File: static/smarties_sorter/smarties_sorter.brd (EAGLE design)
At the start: 160 x 100 mm, 15 parts, among them IC1 MEGA8-P, Q1 16Mhz, Q2 IRLZ44Z

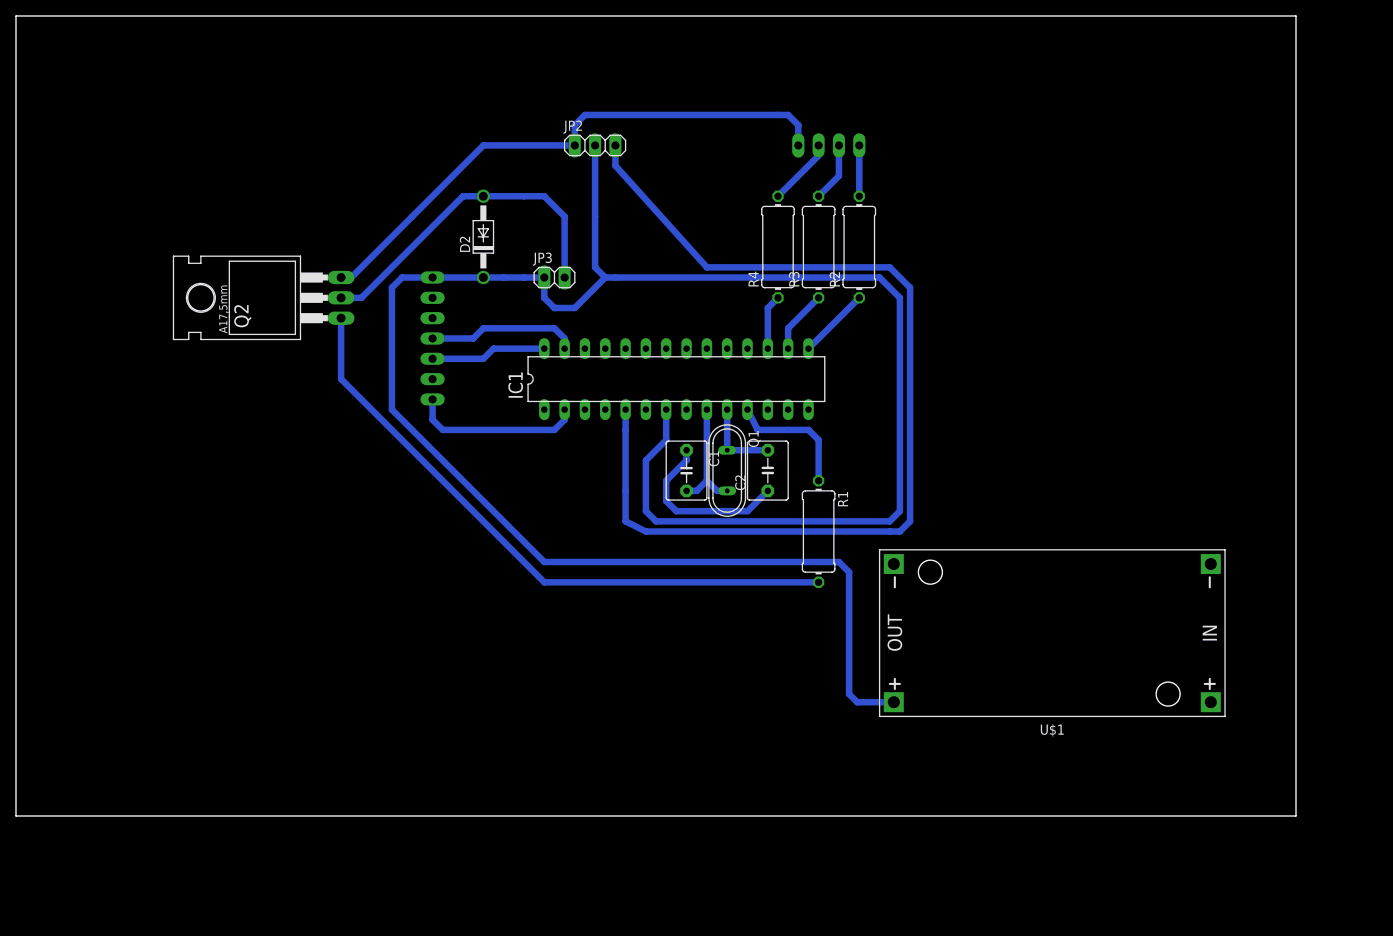
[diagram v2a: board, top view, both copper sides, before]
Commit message: [Smarties sorter] Adds screw clamp for battery
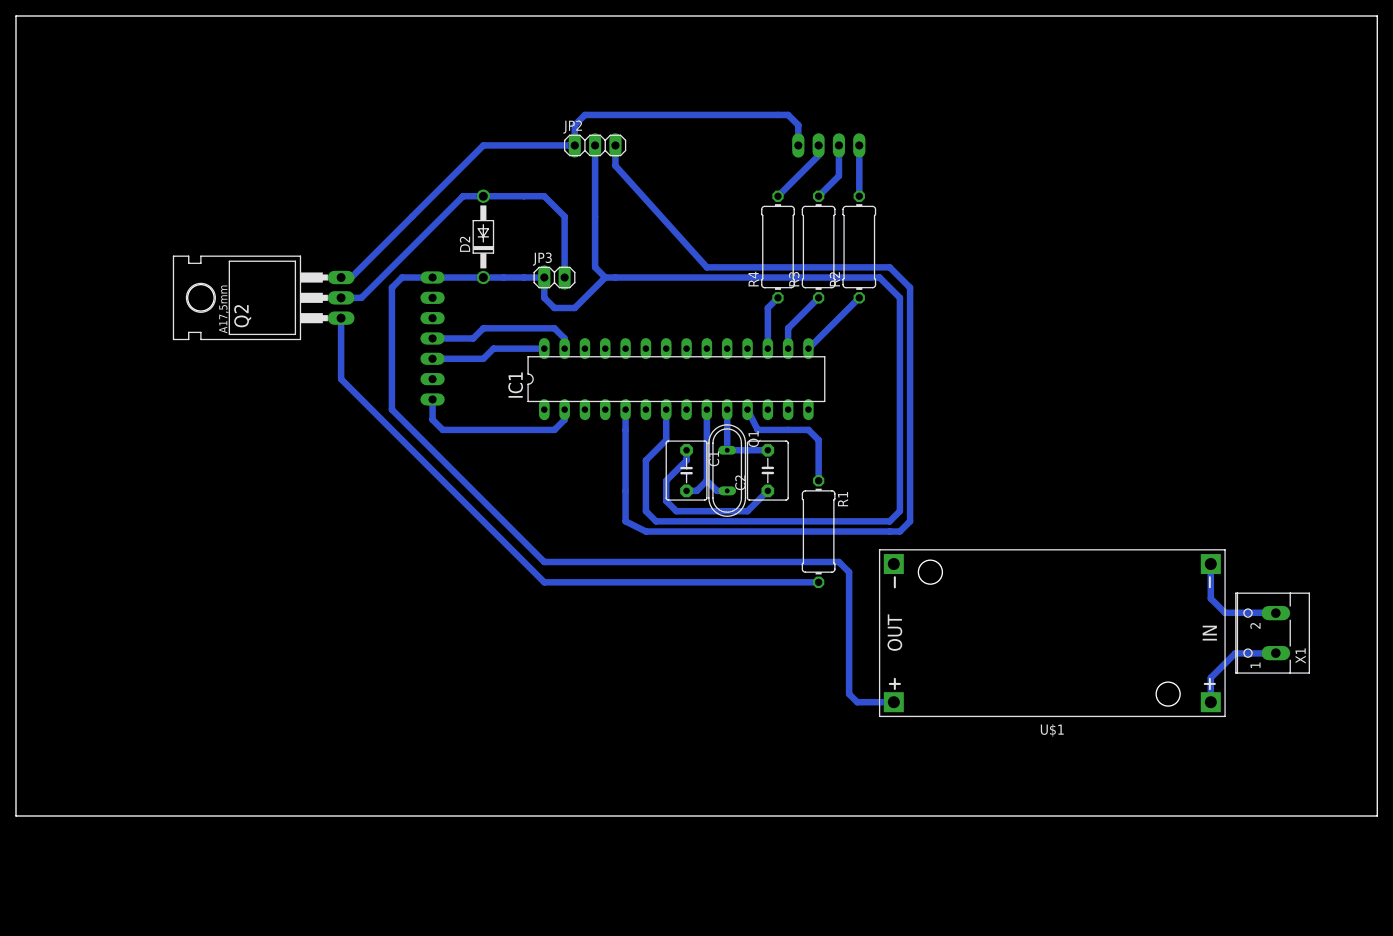
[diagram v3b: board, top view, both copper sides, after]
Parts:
- added X1: (no value), con-wago-500:W237-102
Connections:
- net 12V: now also X1.1
- net 12V_GND: now also X1.2
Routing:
- net 12V_GND: track 0.00 -> 13.2 mm
- net 12V: track 0.00 -> 12.5 mm
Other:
- board size 160 x 100 mm -> 170.2 x 100 mm
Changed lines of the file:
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@@
 <board>
 <plain>
-<wire x1="0" y1="0" x2="160" y2="0" width="0" layer="20"/>
-<wire x1="160" y1="0" x2="160" y2="100" width="0" layer="20"/>
-<wire x1="160" y1="100" x2="0" y2="100" width="0" layer="20"/>
+<wire x1="0" y1="0" x2="170.16" y2="0" width="0" layer="20"/>
+<wire x1="170.16" y1="0" x2="170.16" y2="100" width="0" layer="20"/>
+<wire x1="170.16" y1="100" x2="0" y2="100" width="0" layer="20"/>
 <wire x1="0" y1="100" x2="0" y2="0" width="0" layer="20"/>
 </plain>
@@
 <element name="D2" library="diode" package="DO41-10" value="1N4933" x="58.42" y="72.39" rot="R90"/>
 <element name="U$1" library="diy-modules" package="DC-DC-STEP-DOWN-LM2596" value="DC-DC-STEP-DOWN-LM2596" x="129.54" y="22.86" rot="R180"/>
+<element name="X1" library="con-wago-500" package="W237-102" value="" x="156.21" y="22.86" rot="R90">
+<attribute name="OC_NEWARK" value="70K9898" x="156.21" y="22.86" size="1.778" layer="27" rot="R90" display="off"/>
+<attribute name="MPN" value="237-102" x="156.21" y="22.86" size="1.778" layer="27" rot="R90" display="off"/>
+<attribute name="MF" value="" x="156.21" y="22.86" size="1.778" layer="27" rot="R90" display="off"/>
+<attribute name="OC_FARNELL" value="unknown" x="156.21" y="22.86" size="1.778" layer="27" rot="R90" display="off"/>
+</element>
 </elements>
 <signals>
@@
 <signal name="12V">
 <contactref element="U$1" pad="IN+"/>
+<contactref element="X1" pad="1"/>
+<wire x1="149.352" y1="14.224" x2="149.352" y2="17.272" width="0.8128" layer="16"/>
+<wire x1="149.352" y1="17.272" x2="152.4" y2="20.32" width="0.8128" layer="16"/>
+<wire x1="152.4" y1="20.32" x2="157.44" y2="20.32" width="0.8128" layer="16"/>
+<wire x1="157.44" y1="20.32" x2="157.48" y2="20.36" width="0.8128" layer="16"/>
 </signal>
 <signal name="12V_GND">
 <contactref element="U$1" pad="IN-"/>
+<contactref element="X1" pad="2"/>
+<wire x1="149.352" y1="31.496" x2="149.352" y2="27.178" width="0.8128" layer="16"/>
+<wire x1="149.352" y1="27.178" x2="151.13" y2="25.4" width="0.8128" layer="16"/>
+<wire x1="151.13" y1="25.4" x2="157.44" y2="25.4" width="0.8128" layer="16"/>
+<wire x1="157.44" y1="25.4" x2="157.48" y2="25.36" width="0.8128" layer="16"/>
 </signal>
 </signals>

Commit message: [Smarties Sorter] Adds ground plane.
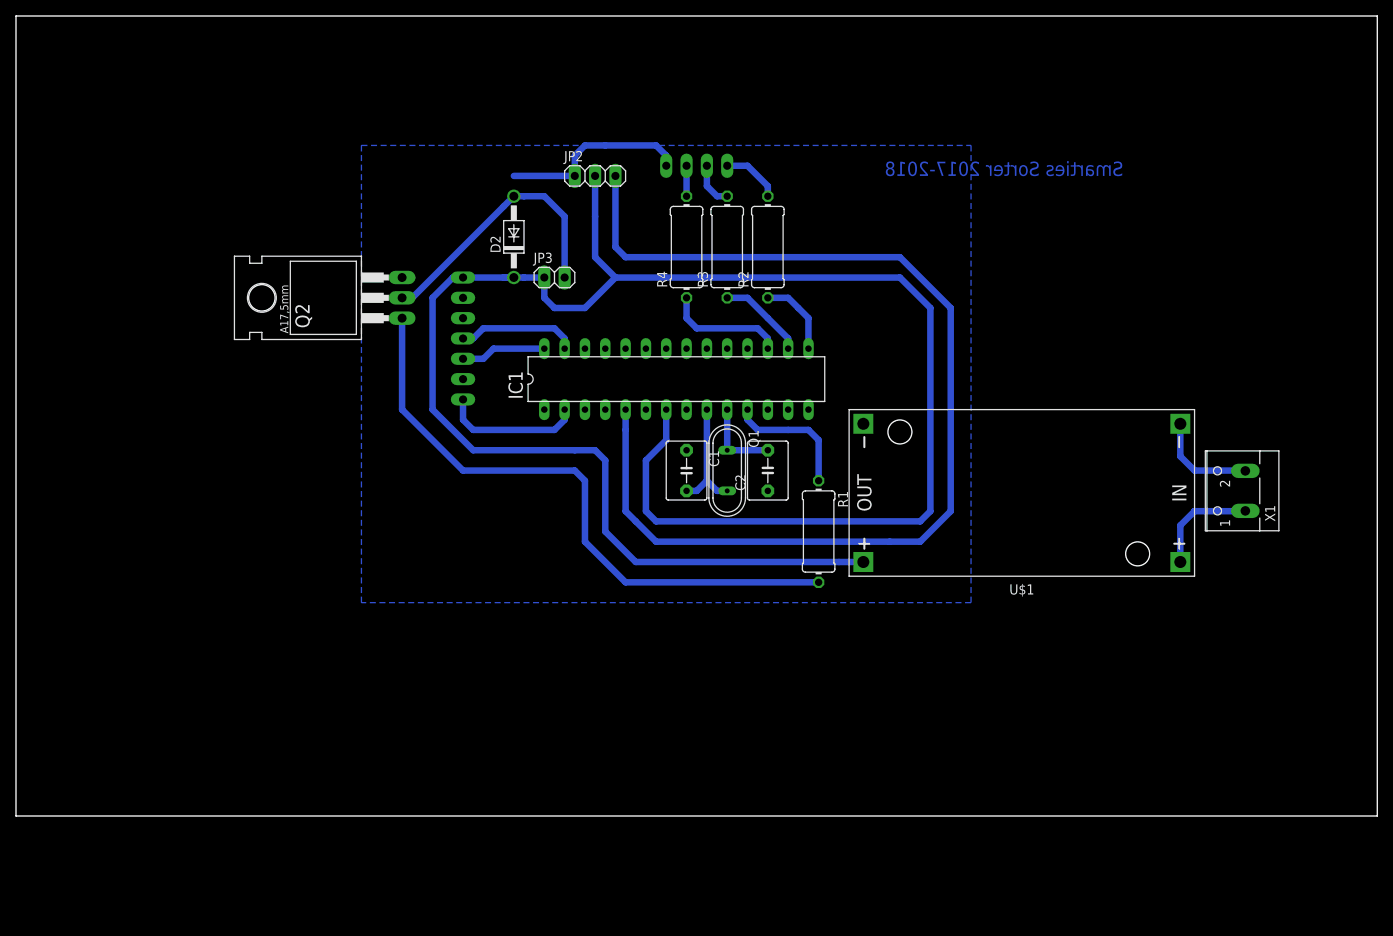
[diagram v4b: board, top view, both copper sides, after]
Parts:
- moved X1 18.2 mm to (152.4, 40.6)
- moved U$1 17.9 mm to (125.7, 40.4)
- moved JP1 16.7 mm to (85.1, 81.3)
- moved R4 11.4 mm to (83.8, 71.1)
- moved R2 11.4 mm to (94.0, 71.1)
- moved R3 11.4 mm to (88.9, 71.1)
- moved Q2 7.62 mm to (41.9, 64.8)
- moved JP4 3.81 mm to (55.9, 59.7)
- moved D2 3.81 mm to (62.2, 72.4)
- moved JP2 3.81 mm to (72.4, 80.0)
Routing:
- net GND: track 91.8 -> 25.2 mm
- net 5V: track 262.0 -> 242.5 mm
- net N$6: track 125.6 -> 135.9 mm
- net N$11: track 6.88 -> 15.0 mm
- net N$7: track 41.9 -> 34.3 mm
- net N$12: track 8.45 -> 3.81 mm
- net N$17: track 18.8 -> 15.0 mm
- net N$16: track 14.5 -> 10.7 mm
- net N$15: track 21.4 -> 17.6 mm
- net N$3: track 7.93 -> 11.0 mm
- net N$10: track 7.40 -> 5.61 mm
- net 12V: track 12.5 -> 13.5 mm
- net N$5: track 6.35 -> 7.40 mm
- net N$4: track 8.98 -> 9.94 mm
- net N$8: track 77.8 -> 76.9 mm
- added copper zone on layer 16, net GND
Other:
- board text added: "Smarties Sorter 2017-2018"

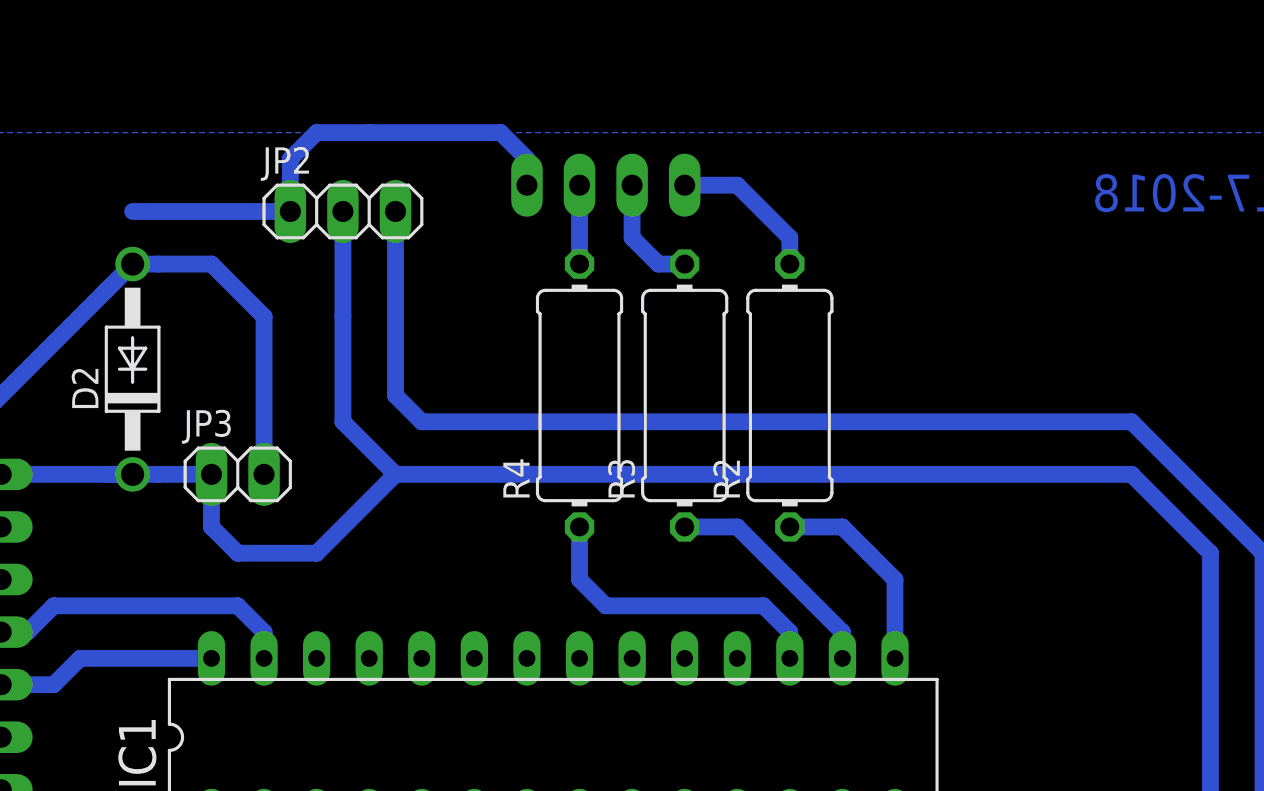
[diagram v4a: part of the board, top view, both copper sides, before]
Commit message: [Smarties Sorter] Connects AVCC to 5V + capacitor
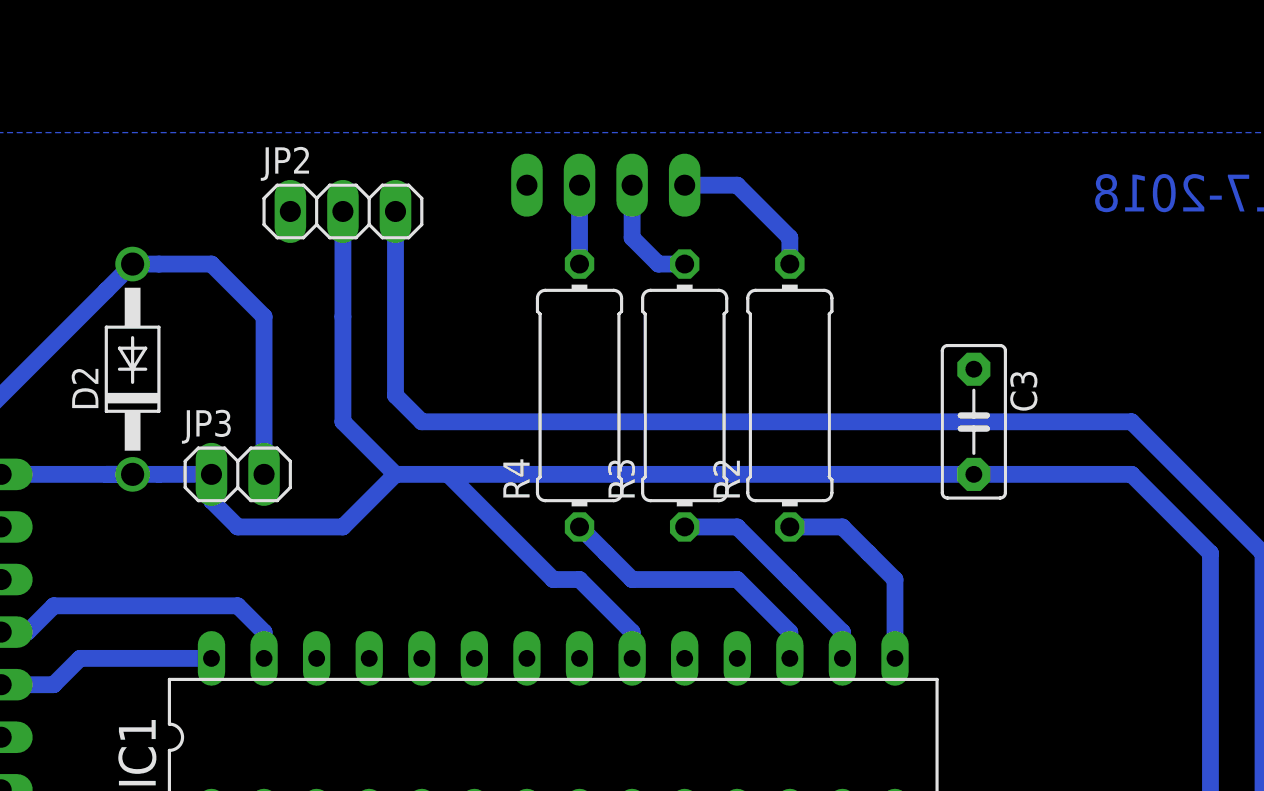
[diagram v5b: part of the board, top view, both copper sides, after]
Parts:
- added C3: 200nF, capacitor-wima:C5B3
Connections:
- removed net AVCC: IC1.20
- net 5V: now also C3.2, IC1.20
- net GND: now also C3.1
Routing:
- net GND: track 25.2 -> 1.27 mm
- net 5V: track 242.5 -> 254.0 mm
- net N$11: track 15.0 -> 13.5 mm
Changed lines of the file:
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@@
 <attribute name="OC_FARNELL" value="unknown" x="152.4" y="40.64" size="1.778" layer="27" rot="R90" display="off"/>
 </element>
+<element name="C3" library="capacitor-wima" package="C5B3" value="200nF" x="102.87" y="69.85" rot="R270"/>
 </elements>
 <signals>
 <signal name="GND">
-<contactref element="IC1" pad="22"/>
 <contactref element="C1" pad="1"/>
 <contactref element="C2" pad="1"/>
@@
 <contactref element="JP4" pad="2"/>
 <wire x1="48.26" y1="67.31" x2="49.53" y2="67.31" width="0.8128" layer="16"/>
-<wire x1="62.23" y1="80.01" x2="69.85" y2="80.01" width="0.8128" layer="16"/>
-<wire x1="69.85" y1="80.01" x2="69.85" y2="82.55" width="0.8128" layer="16"/>
-<wire x1="69.85" y1="82.55" x2="71.12" y2="83.82" width="0.8128" layer="16"/>
-<wire x1="71.12" y1="83.82" x2="73.66" y2="83.82" width="0.8128" layer="16"/>
-<wire x1="73.66" y1="83.82" x2="80.01" y2="83.82" width="0.8128" layer="16"/>
-<wire x1="80.01" y1="83.82" x2="81.28" y2="82.55" width="0.8128" layer="16"/>
-<wire x1="81.28" y1="82.55" x2="81.28" y2="81.28" width="0.8128" layer="16"/>
 <contactref element="U$1" pad="OUT-"/>
 <polygon width="0.8128" layer="16">
@@
 <vertex x="43.18" y="26.67"/>
 </polygon>
-<wire x1="81.28" y1="81.28" x2="81.28" y2="58.42" width="0" layer="19" extent="1-1"/>
-<wire x1="55.88" y1="64.77" x2="49.53" y2="67.31" width="0" layer="19" extent="16-16"/>
-</signal>
-<signal name="AVCC">
-<contactref element="IC1" pad="20"/>
+<contactref element="IC1" pad="22"/>
+<contactref element="C3" pad="1"/>
+<wire x1="49.53" y1="67.31" x2="55.88" y2="64.77" width="0" layer="19" extent="16-16"/>
 </signal>
 <signal name="N$1">
@@
 <contactref element="JP4" pad="1"/>
 <wire x1="72.39" y1="80.01" x2="72.39" y2="74.93" width="0.8128" layer="16"/>
-<wire x1="71.12" y1="63.5" x2="67.31" y2="63.5" width="0.8128" layer="16"/>
-<wire x1="67.31" y1="63.5" x2="66.04" y2="64.77" width="0.8128" layer="16"/>
-<wire x1="66.04" y1="64.77" x2="66.04" y2="66.04" width="0.8128" layer="16"/>
+<wire x1="72.39" y1="64.77" x2="67.31" y2="64.77" width="0.8128" layer="16"/>
+<wire x1="67.31" y1="64.77" x2="66.04" y2="66.04" width="0.8128" layer="16"/>
 <wire x1="66.04" y1="66.04" x2="66.04" y2="67.31" width="0.8128" layer="16"/>
 <wire x1="66.04" y1="67.31" x2="63.5" y2="67.31" width="0.8128" layer="16"/>
@@
 <wire x1="114.3" y1="38.1" x2="114.3" y2="63.5" width="0.8128" layer="16"/>
 <wire x1="114.3" y1="63.5" x2="110.49" y2="67.31" width="0.8128" layer="16"/>
-<wire x1="110.49" y1="67.31" x2="74.93" y2="67.31" width="0.8128" layer="16"/>
-<wire x1="74.93" y1="67.31" x2="71.12" y2="63.5" width="0.8128" layer="16"/>
+<wire x1="110.49" y1="67.31" x2="77.47" y2="67.31" width="0.8128" layer="16"/>
+<wire x1="77.47" y1="67.31" x2="74.93" y2="67.31" width="0.8128" layer="16"/>
+<wire x1="74.93" y1="67.31" x2="72.39" y2="64.77" width="0.8128" layer="16"/>
 <wire x1="72.39" y1="74.93" x2="72.39" y2="69.85" width="0.8128" layer="16"/>
 <wire x1="72.39" y1="69.85" x2="74.93" y2="67.31" width="0.8128" layer="16"/>
 <wire x1="104.14" y1="31.75" x2="105.918" y2="31.75" width="0.8128" layer="16"/>
+<contactref element="IC1" pad="20"/>
+<wire x1="86.36" y1="58.42" x2="86.36" y2="59.69" width="0.8128" layer="16"/>
+<wire x1="86.36" y1="59.69" x2="83.82" y2="62.23" width="0.8128" layer="16"/>
+<wire x1="83.82" y1="62.23" x2="82.55" y2="62.23" width="0.8128" layer="16"/>
+<wire x1="82.55" y1="62.23" x2="77.47" y2="67.31" width="0.8128" layer="16"/>
+<contactref element="C3" pad="2"/>
+<wire x1="110.49" y1="67.31" x2="102.87" y2="67.31" width="0" layer="19" extent="16-16"/>
 </signal>
 <signal name="N$6">
@@
 <contactref element="IC1" pad="17"/>
 <contactref element="R4" pad="1"/>
-<wire x1="83.82" y1="64.77" x2="83.82" y2="62.23" width="0.8128" layer="16"/>
-<wire x1="83.82" y1="62.23" x2="85.09" y2="60.96" width="0.8128" layer="16"/>
-<wire x1="85.09" y1="60.96" x2="92.71" y2="60.96" width="0.8128" layer="16"/>
-<wire x1="92.71" y1="60.96" x2="93.98" y2="59.69" width="0.8128" layer="16"/>
+<wire x1="83.82" y1="64.77" x2="85.09" y2="63.5" width="0.8128" layer="16"/>
+<wire x1="85.09" y1="63.5" x2="86.36" y2="62.23" width="0.8128" layer="16"/>
+<wire x1="86.36" y1="62.23" x2="91.44" y2="62.23" width="0.8128" layer="16"/>
+<wire x1="91.44" y1="62.23" x2="93.98" y2="59.69" width="0.8128" layer="16"/>
 <wire x1="93.98" y1="59.69" x2="93.98" y2="58.42" width="0.8128" layer="16"/>
 </signal>
